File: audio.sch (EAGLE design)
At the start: 42 parts, among them CN1 PH-1X06SG, CN2 PH-1X06RG, CN3 STEREO-3.5-MJ8435, CN4 STEREO-3.5-MJ8435, CN5 DC-JACK-18742, IC1 R5F104BCAFP, IC2 NJM2746E, IC3 NJM2746E, IC4 VBT1-S5-S5-SMT, IC5 NJM2866F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

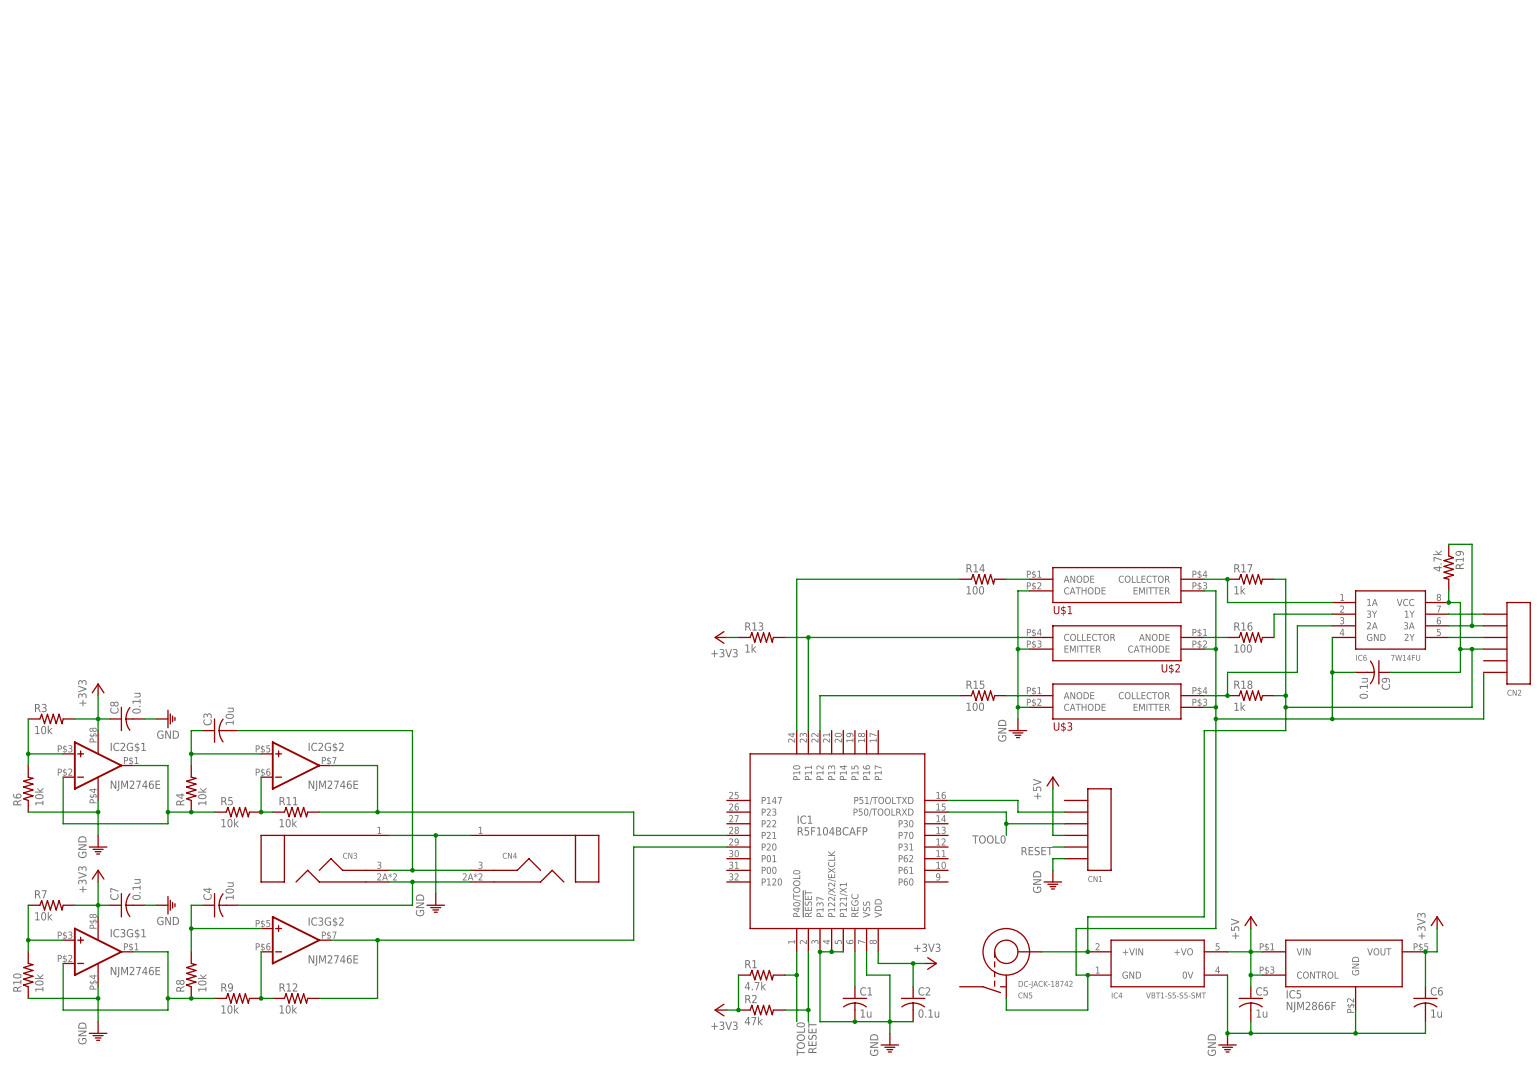
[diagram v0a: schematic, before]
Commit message: Added power chains
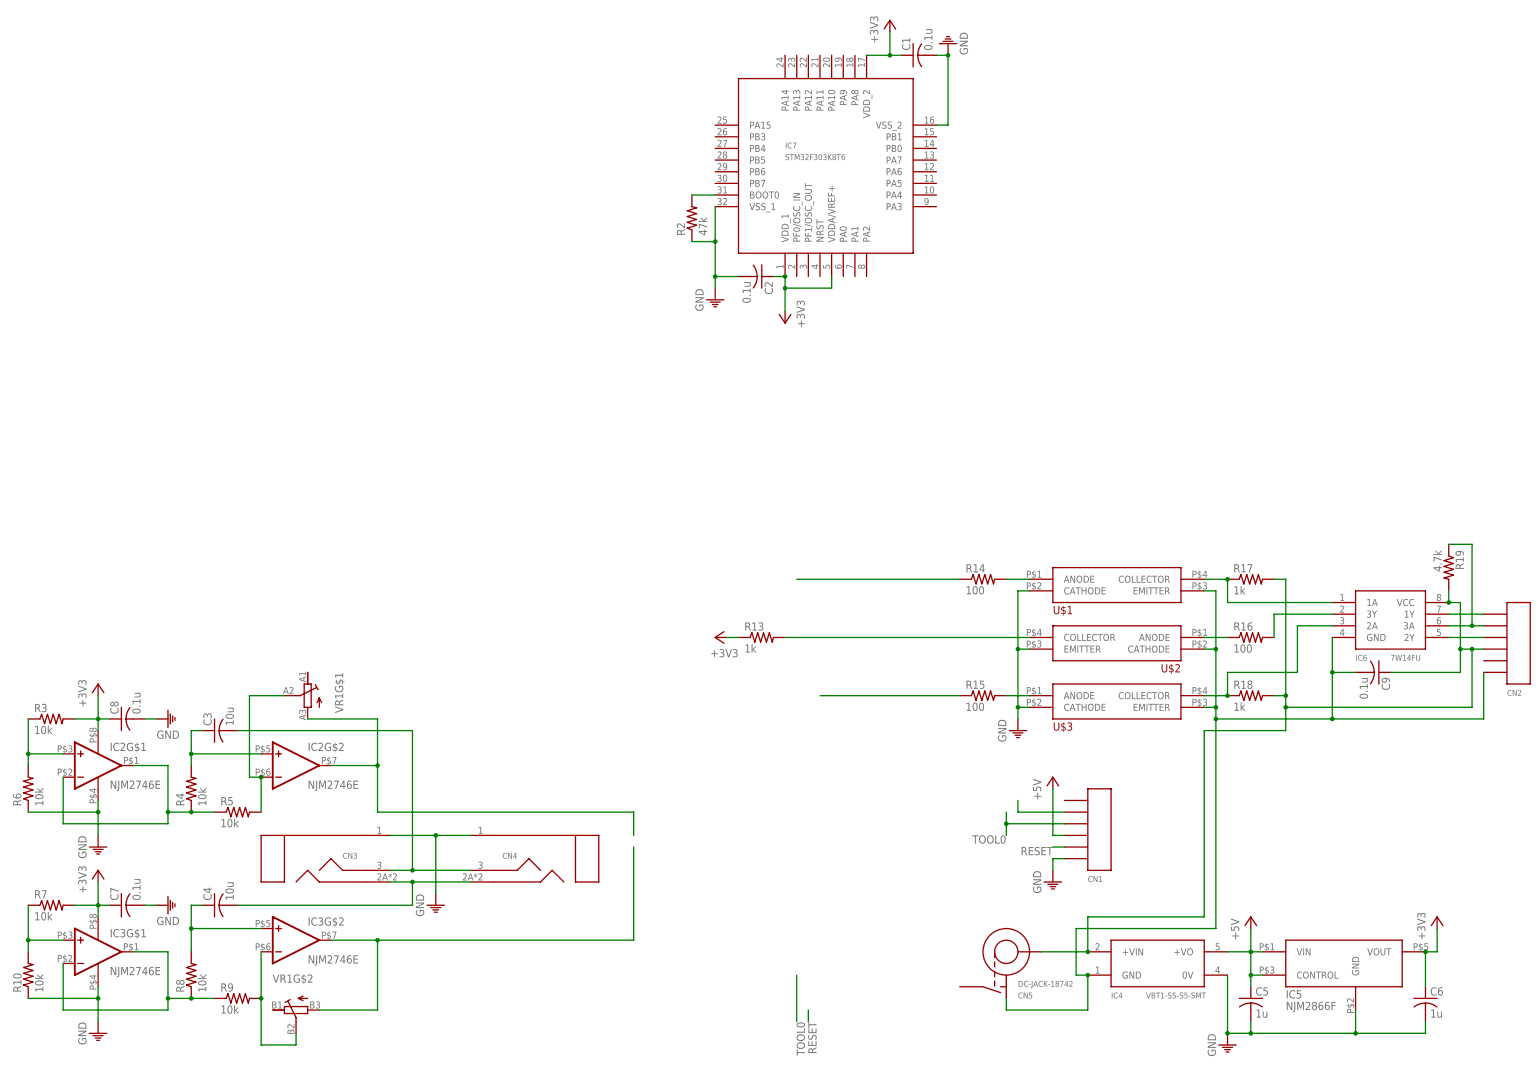
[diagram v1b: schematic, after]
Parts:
- removed IC1: R5F104BCAFP, MyLib:R5F104BCAFP
- removed R1: 4.7k, MyLib:R2012
- removed R11, R12: 10k, MyLib:R2012
- added IC7: STM32F303K8T6, MyLib:STM32F303K8T6
- added VR1: (no value), MyLib:R-TRIM-RK0971220
- C1: value 1u -> 0.1u
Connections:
- net +3V3: now also C1.1, IC7.VDDA/VREF+, IC7.VDD_1, IC7.VDD_2; no longer IC1.VDD, R1.1, R2.1
- net GND: now also IC7.VSS_1, IC7.VSS_2, R2.1; no longer IC1.P121/X1, IC1.P122/X2/EXCLK, IC1.P137, IC1.VSS
- net N$10: now also VR1G$1.E; no longer IC1.P21, R11.2
- net N$14: now also VR1G$2.S; no longer R12.1
- net N$16: now also VR1G$2.E; no longer IC1.P20, R12.2
- net N$17: no longer IC1.P10
- net N$18: no longer IC1.P11
- net N$19: no longer IC1.P12
- net N$2: now also IC7.BOOT0, R2.2; no longer C1.1, IC1.REGC
- net N$4: no longer IC1.P51/TOOLTXD
- net N$9: now also VR1G$1.S; no longer R11.1
- net RESET: no longer IC1.!RESET!, R2.2
- net TOOL0: no longer IC1.P40/TOOL0, IC1.P50/TOOLRXD, R1.2
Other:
- moved on the sheet: C1, C2, R2
